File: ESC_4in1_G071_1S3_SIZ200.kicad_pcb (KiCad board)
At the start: 4 copper layers, 26 x 27 mm, 176 parts, among them J1 Conn_01x08, U1 STM32G071GBU6, U10 NCP81161MNTBG, U11 SIZ200DT-T1-GE3, U12 NCP81161MNTBG, U13 SIZ200DT-T1-GE3, U14 TPS630701, U15 TPS72733DSE, U16 INA185, U17 STM32G071GBU6, U18 NCP81161MNTBG, U19 SIZ200DT-T1-GE3, U2 NCP81161MNTBG, U20 NCP81161MNTBG, U21 STM32G071GBU6, U22 SIZ200DT-T1-GE3, U23 NCP81161MNTBG, U24 SIZ200DT-T1-GE3, U25 NCP81161MNTBG, U26 SIZ200DT-T1-GE3, U27 NCP81161MNTBG, U28 STM32G071GBU6, U29 SIZ200DT-T1-GE3, U3 SIZ200DT-T1-GE3, U30 NCP81161MNTBG, U31 SIZ200DT-T1-GE3, U4 NCP81161MNTBG, U5 SIZ200DT-T1-GE3, U6 NCP81161MNTBG, U7 SIZ200DT-T1-GE3, U8 NCP81161MNTBG, U9 SIZ200DT-T1-GE3

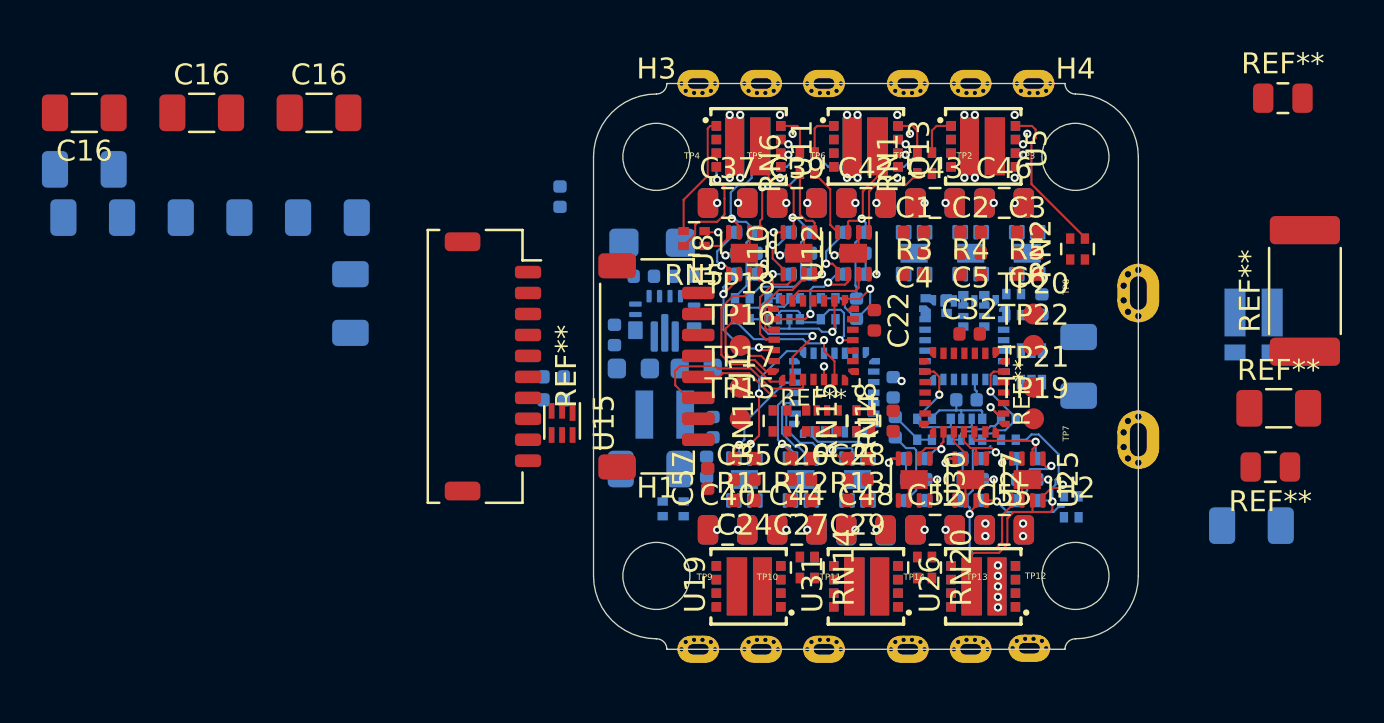
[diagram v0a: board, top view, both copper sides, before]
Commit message: update schematic and layout
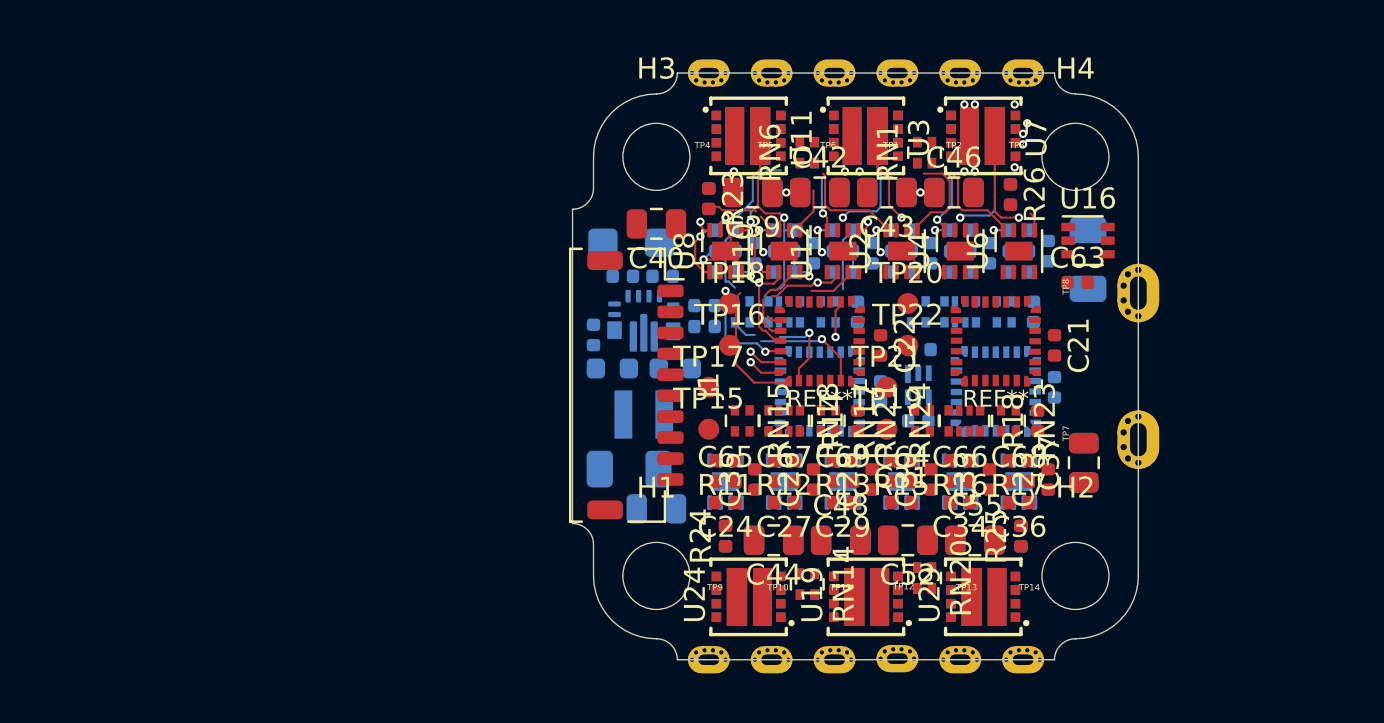
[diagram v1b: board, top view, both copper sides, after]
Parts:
- removed the C16 at (109.9, 62.9)
- removed the C16 at (104.3, 62.9)
- removed the C16 at (98.7, 65.6)
- removed the C16 at (104.7, 67.9)
- removed the C16 at (111.4, 72.0)
- removed the C16 at (110.3, 67.9)
- removed the C16 at (98.7, 62.9)
- removed the C16 at (154.4, 82.6)
- removed the C16 at (99.1, 67.9)
- removed REF**: R_2512_6332Metric, Resistor_SMD:R_2512_6332Metric
- removed REF**: JST_SHL_SM10B-SHLS-TF_1x10-1MP_P1.00mm_Horizontal, Connector_JST:JST_SHL_SM10B-SHLS-TF_1x10-1MP_P1.00mm_Horizontal
- removed REF** (x2): R_1206_3216Metric, Resistor_SMD:R_1206_3216Metric
- removed REF** (x2): C_0805_2012Metric_dense, 11_PSoC_FC_whoop:C_0805_2012Metric_dense
- removed REF**: C_0402_1005Metric, Capacitor_SMD:C_0402_1005Metric
- removed RN13, RN16, RN2, RN5: 10R0, 11_PSoC_FC_whoop:R_Array_Convex_2x0402_dense
- added C58: 10u, Capacitor_SMD:C_0402_1005Metric, B.Cu at (140.5, 69.5)
- added C59: 10u, Capacitor_SMD:C_0402_1005Metric, B.Cu at (132.1, 69.5)
- added C60: 10u, Capacitor_SMD:C_0402_1005Metric, B.Cu at (137.7, 69.5)
- added C61: 10u, Capacitor_SMD:C_0402_1005Metric, B.Cu at (134.9, 69.5)
- added C62: 10u, Capacitor_SMD:C_0402_1005Metric, B.Cu at (143.3, 69.5)
- added C63: 100n, Capacitor_SMD:C_0402_1005Metric, F.Cu at (146.1, 71.0)
- added C64: 10u, Capacitor_SMD:C_0402_1005Metric, F.Cu at (137.7, 80.5)
- added C65: 10u, Capacitor_SMD:C_0402_1005Metric, F.Cu at (129.3, 80.5)
- added C66: 10u, Capacitor_SMD:C_0402_1005Metric, F.Cu at (140.5, 80.5)
- added C67: 10u, Capacitor_SMD:C_0402_1005Metric, F.Cu at (132.1, 80.5)
- added C68: 10u, Capacitor_SMD:C_0402_1005Metric, F.Cu at (143.3, 80.5)
- added C69: 10u, Capacitor_SMD:C_0402_1005Metric, F.Cu at (134.9, 80.5)
- added R19: 10R0, Resistor_SMD:R_0402_1005Metric, B.Cu at (128.5, 67.0)
- added R20: 10R0, Resistor_SMD:R_0402_1005Metric, B.Cu at (129.3, 83.1)
- added R21: 10R0, Resistor_SMD:R_0402_1005Metric, B.Cu at (143.4, 83.1)
- added R22: 10R0, Resistor_SMD:R_0402_1005Metric, B.Cu at (142.9, 66.8)
- added R23: 10R0, Resistor_SMD:R_0402_1005Metric, F.Cu at (128.5, 67.0)
- added R24: 10R0, Resistor_SMD:R_0402_1005Metric, F.Cu at (129.3, 83.1)
- added R25: 10R0, Resistor_SMD:R_0402_1005Metric, F.Cu at (143.4, 83.1)
- added R26: 10R0, Resistor_SMD:R_0402_1005Metric, F.Cu at (142.9, 66.8)
- C1, C2, C3, C32, C4, C5, C57, C6, R3, R4, R5, U13, U15, U25, U26, U27, U28, U30, U31, U5: moved to B.Cu
- C21, C23, C30, C31, C33, C34, C36, R15, R16, R17, R18, RN21, RN23, RN24, U1, U2, U24, U29, U3, U4, U6, U7: moved to F.Cu
- J1: value Conn_01x08 -> Conn_01x10; footprint Connector_JST:JST_SH_SM08B-SRSS-TB_1x08-1MP_P1.00mm_Horizontal -> 11_PSoC_FC_whoop:JST_SHL_SM10B-SHLS-TF_1x10-1MP_P1.00mm_Horizontal_dense
- R1: value R_Shunt -> 0m5; footprint Resistor_SMD:R_Shunt_Vishay_WSKW0612 -> Resistor_SMD:R_1206_3216Metric
- U16: value INA185 -> INA186A2; footprint Package_TO_SOT_SMD:SOT-563 -> Package_TO_SOT_SMD:SOT-363_SC-70-6; moved to F.Cu
- moved C37 21.0 mm to (146.4, 79.6), turned to 90 degrees
- moved C50 21.0 mm to (146.4, 79.6), turned to 90 degrees
- moved C19 17.5 mm to (138.6, 74.2), turned to 180 degrees
- moved C18 17.4 mm to (138.5, 77.6), turned to 180 degrees
- moved U15 17.1 mm to (138.5, 75.9)
- moved C40 15.0 mm to (126.0, 68.2), turned to 180 degrees
- moved C57 10.9 mm to (129.3, 69.5), turned to 0 degrees
- moved R1 8.49 mm to (146.6, 69.9)
- moved C20 7.70 mm to (128.3, 72.1), turned to 180 degrees
- moved TP19 7.02 mm to (137.0, 78.0)
- moved TP21 7.00 mm to (137.0, 76.0)
- moved R18 6.81 mm to (144.2, 77.6)
- moved U16 6.58 mm to (146.6, 69.0), turned to 0 degrees
- moved TP12 6.32 mm to (137.5, 89.0)
- moved C23 6.30 mm to (144.7, 80.4), turned to 90 degrees
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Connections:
- TP8 pad 1: Net-(R1-Pad4) -> Net-(R1-Pad2)
- U16 pad 4: Net-(R1-Pad2) -> GND
- U16 pad 5: Net-(R1-Pad3) -> Net-(R1-Pad2)
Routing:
- net GND: track 26.2 -> 3.05 mm, vias 33 -> 10
- net /ESC3_A: track 13.6 -> 0.00 mm, vias 1 -> 0
- net /ESC2_IN: track 9.07 -> 0.00 mm
- net /ESC3_B: track 8.59 -> 0.00 mm, vias 1 -> 0
- net +5V: track 13.2 -> 4.60 mm, vias 6 -> 2
- net /ESC1_B_GL: track 7.33 -> 0.00 mm
- net /ESC3_Y: track 6.84 -> 0.00 mm, vias 1 -> 0
- net /ESC4_A_EN: track 6.64 -> 0.00 mm, vias 2 -> 0
- net /ESC4_C_PWM: track 6.10 -> 0.00 mm, vias 1 -> 0
- net /ESC3_MA: track 5.86 -> 0.00 mm, vias 1 -> 0
- net /ESC2_B_GH: track 5.84 -> 0.00 mm
- net /ESC4_A_PWM: track 5.77 -> 0.00 mm, vias 1 -> 0
- net /ESC1_B: track 0.00 -> 5.35 mm, vias 0 -> 1
- net /ESC2_MC: track 5.35 -> 0.00 mm, vias 1 -> 0
- net /ESC2_A_GH: track 5.27 -> 0.00 mm, vias 1 -> 0
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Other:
- board size 26 x 27 mm -> 27 x 28 mm
- board text removed: "LAYOUT C"

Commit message: update design files
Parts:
- added R27: 1k, Resistor_SMD:R_0402_1005Metric, B.Cu at (129.0, 74.7)
- added R28: 1k, Resistor_SMD:R_0402_1005Metric, F.Cu at (138.5, 75.9)
- added R29: 1k, Resistor_SMD:R_0402_1005Metric, B.Cu at (136.9, 73.8)
- added R30: 1k, Resistor_SMD:R_0402_1005Metric, F.Cu at (139.5, 75.9)
- added RN2: 1k, 11_PSoC_FC_whoop:R_Array_Convex_4x0402_dense, B.Cu at (128.7, 77.2)
- C20, R2: moved to F.Cu
- moved TP16 2.00 mm to (129.5, 72.0)
- moved TP18 2.00 mm to (129.5, 74.0)
- moved C37 1.27 mm to (146.2, 80.8)
- moved C50 1.27 mm to (146.2, 80.8)
- moved R18 1.02 mm to (145.2, 77.8)
- moved RN21 1.02 mm to (139.7, 77.8)
- moved RN23 1.02 mm to (143.8, 77.8)
- moved RN24 1.02 mm to (141.7, 77.8)
- moved C21 1.00 mm to (146.0, 74.0)
- moved C32 1.00 mm to (146.0, 76.0)
- moved R6 1.00 mm to (145.0, 72.4)
- moved RN7 1.00 mm to (143.6, 72.4)
- moved RN8 1.00 mm to (139.5, 72.4)
- moved RN9 1.00 mm to (141.5, 72.4)
- moved TP7 1.00 mm to (150.0, 78.5)
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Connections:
- J1 pad 5: /ESC1_IN -> Net-(J1-Pad5)
- J1 pad 6: /ESC2_IN -> Net-(J1-Pad6)
- J1 pad 7: /ESC3_IN -> Net-(J1-Pad7)
- J1 pad 8: /ESC4_IN -> Net-(J1-Pad8)
- RN24 pad 5: /ESC3_Y -> GND
- RN24 pad 6: GND -> /ESC3_Y
- RN24 pad 7: /ESC3_Y -> GND
- RN24 pad 8: GND -> /ESC3_Y
- RN9 pad 5: /ESC1_Y -> GND
- RN9 pad 6: GND -> /ESC1_Y
- RN9 pad 7: /ESC1_Y -> GND
- RN9 pad 8: GND -> /ESC1_Y
- U1 pad 26: /ESCx_tele -> Net-(R30-Pad2)
- U17 pad 26: /ESCx_tele -> Net-(R28-Pad2)
- U21 pad 26: /ESCx_tele -> Net-(R27-Pad2)
- U28 pad 26: /ESCx_tele -> Net-(R29-Pad2)
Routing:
- net GND: track 3.05 -> 25.0 mm, vias 10 -> 15
- net +5V: track 4.60 -> 17.7 mm, vias 2 -> 6
- net /ESC1_MA: track 0.00 -> 10.3 mm, vias 0 -> 1
- net /ESC1_A_PWM: track 0.00 -> 8.96 mm, vias 0 -> 2
- net /ESC1_MB: track 0.00 -> 8.31 mm, vias 0 -> 1
- net /ESC1_A_EN: track 0.00 -> 7.92 mm, vias 0 -> 2
- net /ESC3_A_PWM: track 0.00 -> 7.37 mm, vias 0 -> 1
- net /ESC1_Y: track 0.00 -> 6.41 mm, vias 0 -> 1
- net /ESC1_C: track 4.87 -> 11.2 mm
- net /ESC1_A: track 4.37 -> 10.5 mm
- net /ESC1_B_PWM: track 0.00 -> 6.03 mm, vias 0 -> 1
- net /ESC1_B: track 5.35 -> 10.8 mm
- net /ESC1_SWDIO: track 0.00 -> 5.00 mm
- net /ESC1_C_PWM: track 0.00 -> 4.92 mm, vias 0 -> 1
- net /ESC3_B_PWM: track 0.00 -> 4.90 mm, vias 0 -> 1
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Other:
- board size 27 x 28 mm -> 28 x 28 mm

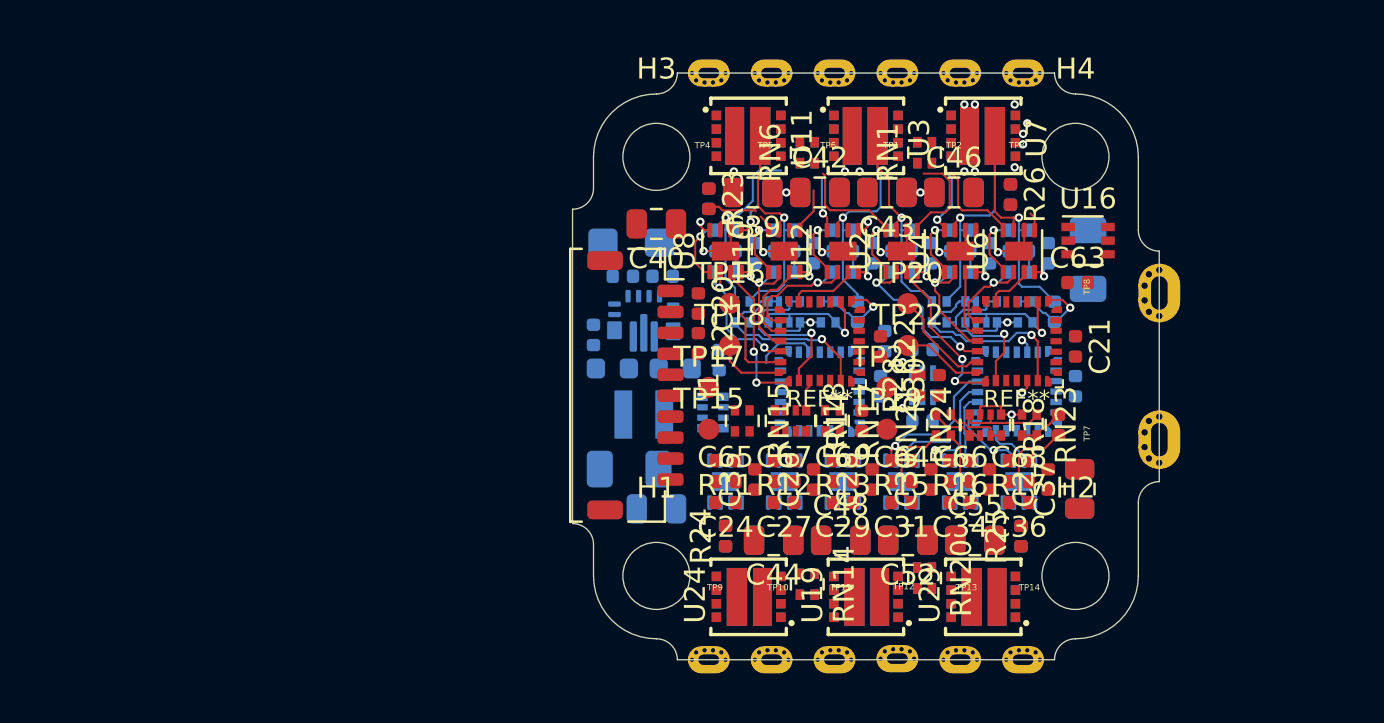
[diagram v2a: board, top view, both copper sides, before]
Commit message: update schematic and layout
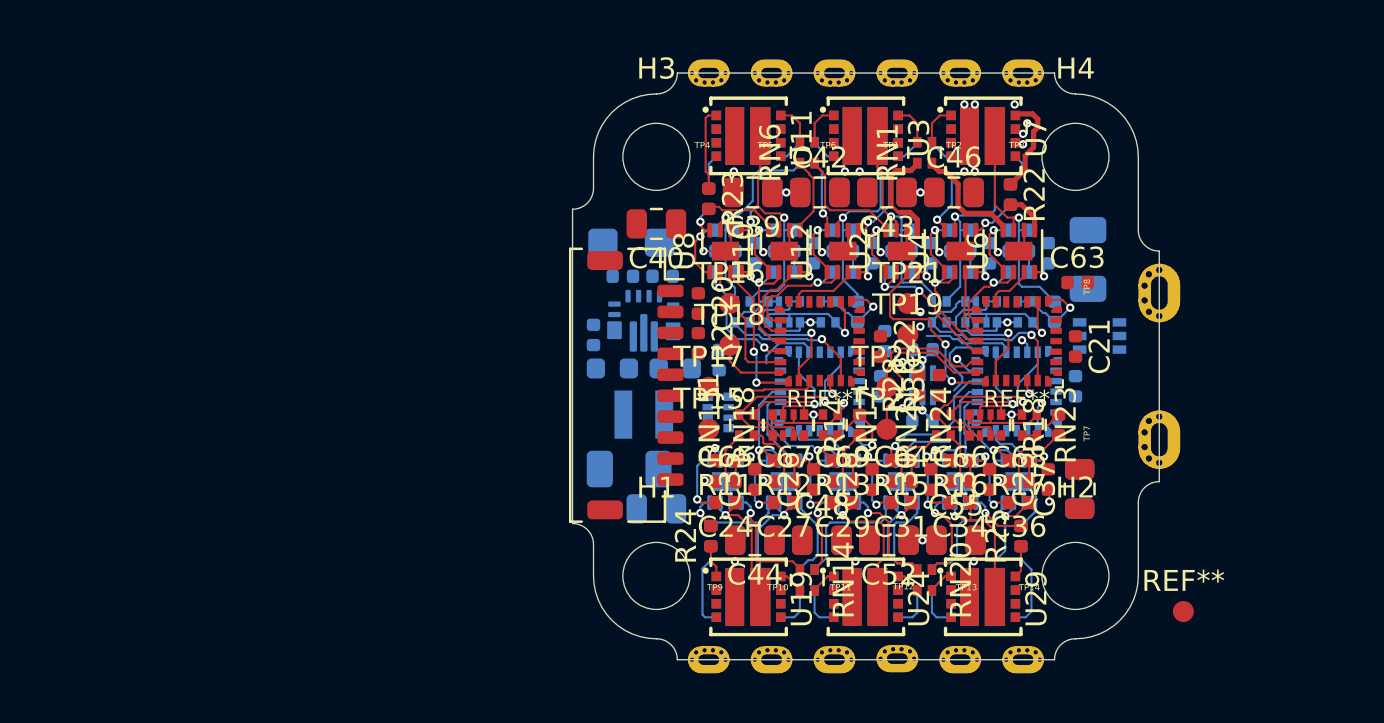
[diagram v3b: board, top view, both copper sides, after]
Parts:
- added REF**: TestPoint_Pad_D1.0mm_dense, 11_PSoC_FC_whoop:TestPoint_Pad_D1.0mm_dense, F.Cu at (151.2, 86.7)
- R22: moved to F.Cu
- R26, U16: moved to B.Cu
- moved U19 5.60 mm to (130.4, 86.0), turned to 270 degrees
- moved U24 5.60 mm to (136.0, 86.0), turned to 270 degrees
- moved U26 5.60 mm to (136.0, 86.0), turned to 90 degrees
- moved U31 5.60 mm to (141.6, 86.0), turned to 90 degrees
- moved TP19 4.61 mm to (138.0, 73.5)
- moved U16 4.58 mm to (147.2, 73.5)
- moved TP20 4.12 mm to (137.0, 76.0)
- moved TP21 4.12 mm to (138.0, 72.0)
- moved TP22 4.12 mm to (137.0, 78.0)
- moved C41 0.90 mm to (130.7, 83.3)
- moved C44 0.90 mm to (130.7, 83.3)
- moved C45 0.90 mm to (133.9, 83.3)
- moved C48 0.90 mm to (133.9, 83.3)
- moved C49 0.90 mm to (137.1, 83.3)
- moved C52 0.90 mm to (137.1, 83.3)
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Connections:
- R20 pad 1: /ESC4_B_GL -> /ESC4_B_GH
- R20 pad 2: /ESC4_C_DRVL -> /ESC4_B_DRVH
- R21 pad 1: /ESC3_A_GH -> /ESC3_C_GL
- R21 pad 2: /ESC3_A_DRVH -> /ESC3_C_DRVL
- R24 pad 1: /ESC4_C_GL -> /ESC4_A_GH
- R24 pad 2: /ESC4_B_DRVL -> /ESC4_A_DRVH
- R25 pad 1: /ESC3_B_GH -> /ESC3_B_GL
- R25 pad 2: /ESC3_B_DRVH -> /ESC3_B_DRVL
- RN1 pad 1: /ESC2_C_DRVL -> /ESC1_A_DRVL
- RN1 pad 2: /ESC1_B_DRVH -> /ESC1_C_DRVH
- RN1 pad 3: /ESC1_B_GH -> /ESC1_C_GH
- RN1 pad 4: /ESC2_C_GL -> /ESC1_A_GL
- RN14 pad 1: /ESC4_A_DRVL -> /ESC4_C_DRVH
- RN14 pad 2: /ESC4_B_DRVH -> /ESC4_A_DRVL
- RN14 pad 3: /ESC4_B_GH -> /ESC4_A_GL
- RN14 pad 4: /ESC4_A_GL -> /ESC4_C_GH
- RN19 pad 1: /ESC3_C_DRVH -> /ESC3_A_DRVL
- RN19 pad 2: /ESC3_A_DRVL -> /ESC3_C_DRVH
- RN19 pad 3: /ESC3_A_GL -> /ESC3_C_GH
- RN19 pad 4: /ESC3_C_GH -> /ESC3_A_GL
- RN20 pad 1: /ESC3_B_DRVL -> /ESC3_B_DRVH
- RN20 pad 2: /ESC4_A_DRVH -> /ESC4_C_DRVL
- RN20 pad 3: /ESC4_A_GH -> /ESC4_C_GL
- RN20 pad 4: /ESC3_B_GL -> /ESC3_B_GH
- RN22 pad 1: /ESC4_C_DRVH -> /ESC4_B_DRVL
- RN22 pad 2: /ESC3_C_DRVL -> /ESC3_A_DRVH
- RN22 pad 3: /ESC3_C_GL -> /ESC3_A_GH
- RN22 pad 4: /ESC4_C_GH -> /ESC4_B_GL
- RN3 pad 1: /ESC1_C_DRVH -> /ESC1_B_DRVH
- RN3 pad 2: /ESC1_A_DRVL -> /ESC2_C_DRVL
- RN3 pad 3: /ESC1_A_GL -> /ESC2_C_GL
- RN3 pad 4: /ESC1_C_GH -> /ESC1_B_GH
- RN4 pad 1: /ESC1_A_DRVH -> /ESC2_C_DRVH
- RN4 pad 4: /ESC1_A_GH -> /ESC2_C_GH
- RN6 pad 2: /ESC2_C_DRVH -> /ESC1_A_DRVH
- RN6 pad 3: /ESC2_C_GH -> /ESC1_A_GH
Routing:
- net GND: track 25.0 -> 53.2 mm, vias 15 -> 26
- net +5V: track 17.7 -> 35.8 mm, vias 6 -> 13
- net /ESC4_C: track 0.00 -> 10.9 mm, vias 0 -> 1
- net /ESC4_B: track 0.00 -> 10.8 mm, vias 0 -> 1
- net /ESC4_A: track 0.00 -> 10.1 mm, vias 0 -> 1
- net /ESC4_MA: track 0.00 -> 9.81 mm, vias 0 -> 1
- net /ESC4_MB: track 0.00 -> 9.05 mm, vias 0 -> 1
- net /ESC3_MA: track 2.57 -> 10.1 mm, vias 0 -> 1
- net /ESC3_B: track 3.59 -> 10.4 mm, vias 0 -> 1
- net /ESC3_C: track 4.78 -> 11.1 mm, vias 0 -> 1
- net /ESC4_Y: track 0.00 -> 6.13 mm, vias 0 -> 1
- net /ESC3_MB: track 3.05 -> 9.12 mm, vias 0 -> 1
- net /ESC3_A: track 4.67 -> 10.7 mm, vias 0 -> 1
- net /ESC3_A_DRVH: track 0.00 -> 6.01 mm
- net /ESC4_C_PWM: track 0.00 -> 5.98 mm, vias 0 -> 1
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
